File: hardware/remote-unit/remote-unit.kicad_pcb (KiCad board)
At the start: 2 copper layers, 100.6 x 51.3 mm, 49 parts, among them J1 SOL_A, J2 RF Module, J3 ICSP, J4 IO, J5 SOL_B, J6 PWR 12V, J7 UART, J8 I2C, SW1 RESET, U1 ATmega328P-AU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

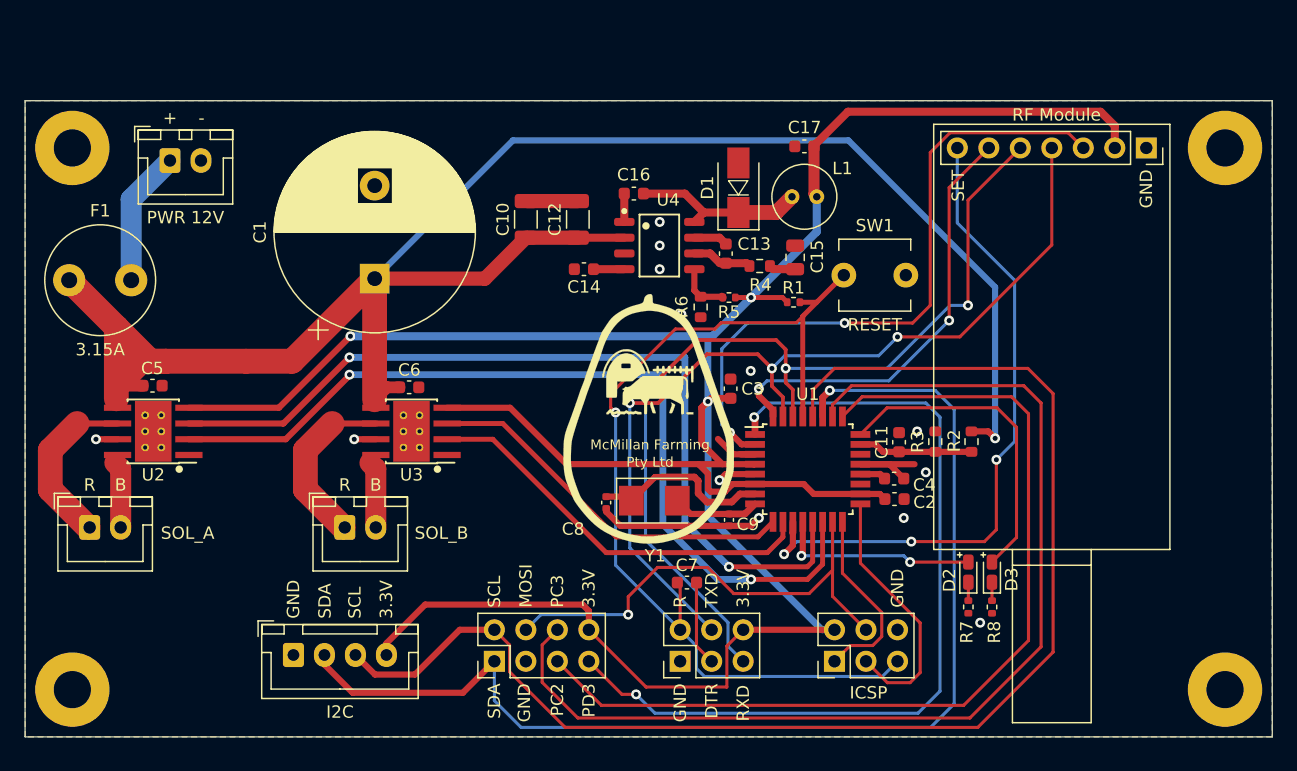
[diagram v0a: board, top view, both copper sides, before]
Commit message: Update inductor footprint on remote unit
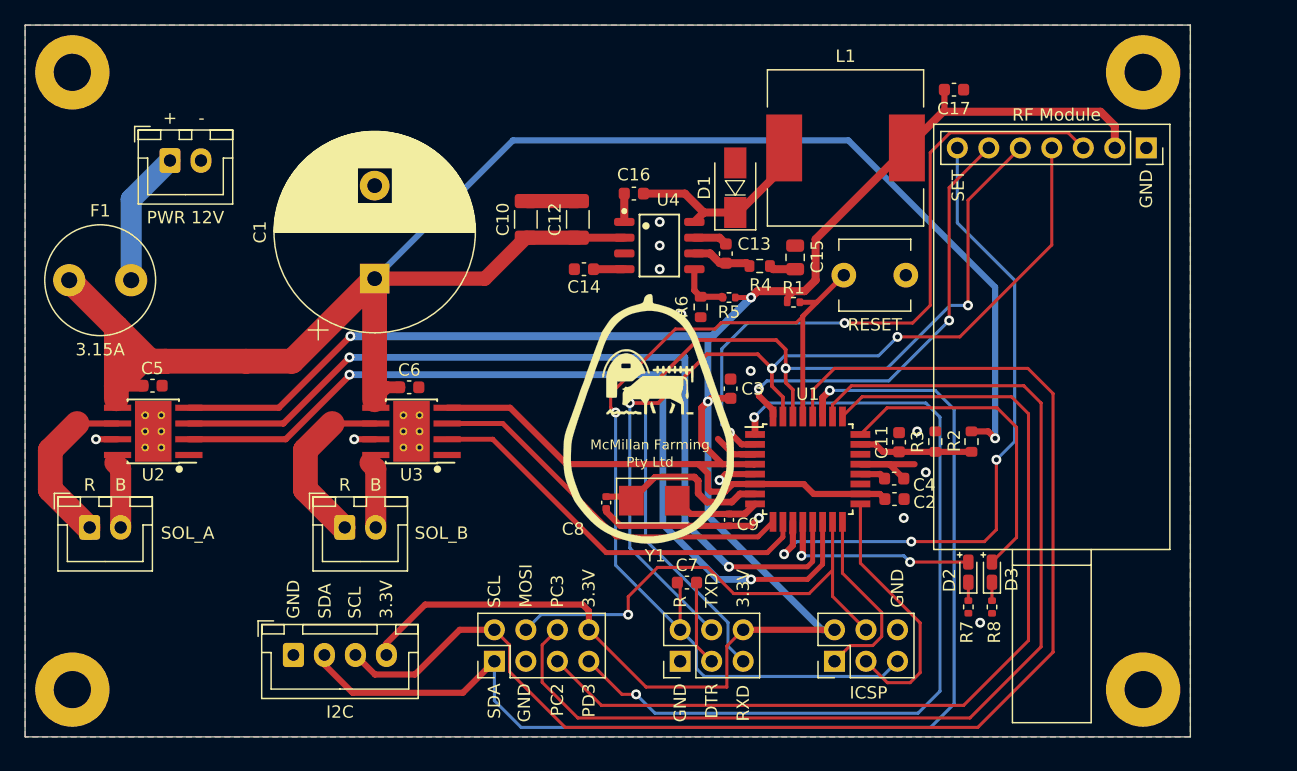
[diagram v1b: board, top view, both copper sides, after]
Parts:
- L1: footprint Capacitor_THT:C_Radial_D5.0mm_H7.0mm_P2.00mm -> Inductor_SMD:L_12x12mm_H8mm
- moved C17 12.9 mm to (157.2, 71.8), turned to 0 degrees
- moved H4 8.99 mm to (172.5, 70.4)
- moved H1 6.60 mm to (172.5, 120.1)
- moved H3 6.10 mm to (86.1, 70.4)
- moved L1 5.84 mm to (148.5, 76.5)
- moved D1 0.25 mm to (139.6, 79.7)
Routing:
- net Net-(C16-Pad1): track 14.2 -> 17.5 mm
- net +3V3: track 222.1 -> 220.5 mm
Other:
- board size 100.6 x 51.3 mm -> 94 x 57.4 mm

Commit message: Add boost converter for solar panel
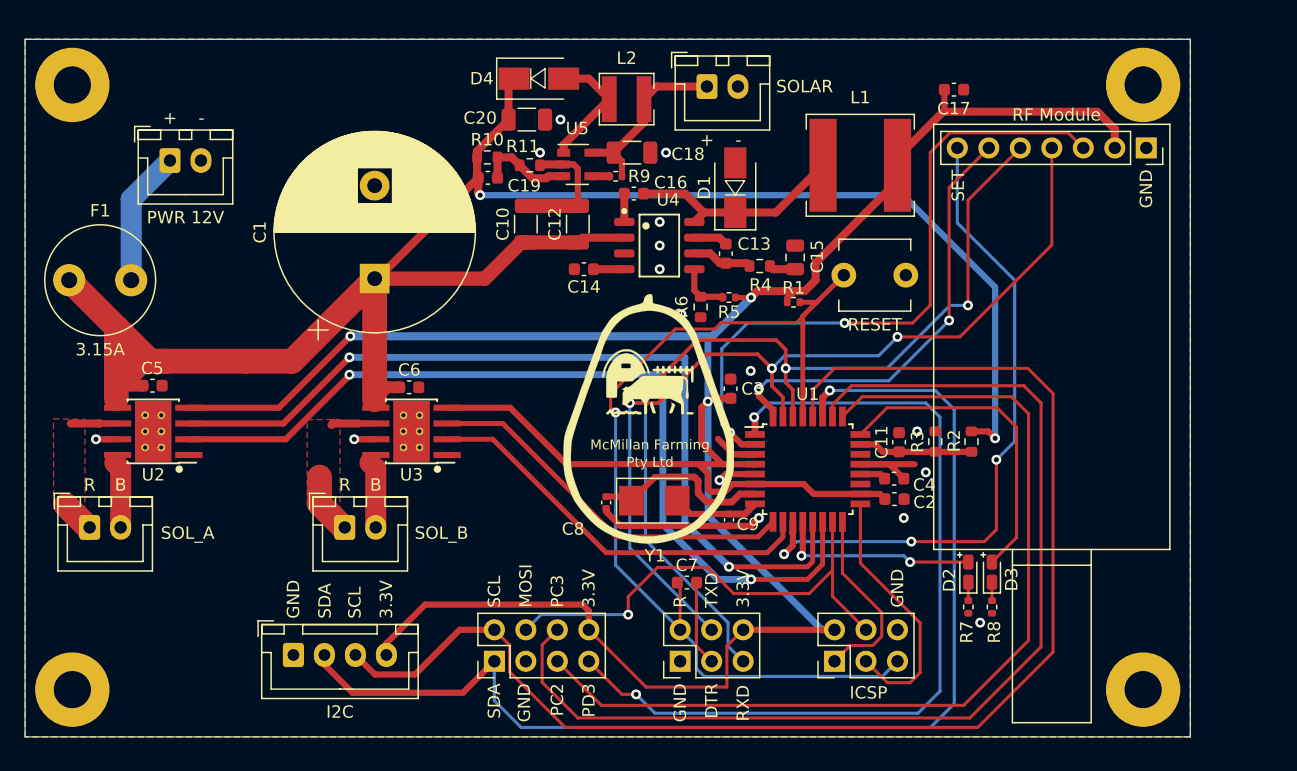
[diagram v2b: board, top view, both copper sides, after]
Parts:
- added C18: 10uF, Capacitor_SMD:C_1206_3216Metric, F.Cu at (131.2, 76.8)
- added C19: 200pF, Capacitor_SMD:C_0603_1608Metric, F.Cu at (119.6, 78.9)
- added C20: 10uF, Capacitor_SMD:C_1206_3216Metric, F.Cu at (122.8, 74.2)
- added D4: 550mV 1A, Diode_SMD:D_SMA, F.Cu at (123.7, 70.9)
- added J9: SOLAR, Connector_JST:JST_XH_B2B-XH-A_1x02_P2.50mm_Vertical, F.Cu at (137.3, 71.5)
- added L2: 10uH, lib:L_4x4mm_H2mm, F.Cu at (130.8, 72.5)
- added R10: 130k, Resistor_SMD:R_0603_1608Metric, F.Cu at (119.6, 77.2)
- added R11: 13k, Resistor_SMD:R_0603_1608Metric, F.Cu at (123.0, 77.9)
- added R9: 51k, Resistor_SMD:R_0402_1005Metric, F.Cu at (129.9, 78.7)
- added U5: LM27313XMF, Package_TO_SOT_SMD:SOT-23-5, F.Cu at (126.8, 77.8)
- L1: footprint Inductor_SMD:L_12x12mm_H8mm -> lib:L_8x8mm_H4mm
- moved L1 1.84 mm to (149.7, 77.9)
- moved H3 1.02 mm to (86.1, 71.4)
- moved H4 1.02 mm to (172.5, 71.4)
- moved C10 0.38 mm to (122.7, 82.6)
- moved C12 0.38 mm to (126.9, 82.6)
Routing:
- net /SOLAR: track 0.00 -> 14.8 mm
- net Net-(D4-Pad2): track 0.00 -> 10.2 mm
- net Net-(C19-Pad2): track 0.00 -> 7.75 mm
- net /SOL_A1: track 13.8 -> 6.29 mm
- net +12V: track 149.4 -> 156.9 mm, vias 1 -> 2
- net GND: track 39.7 -> 45.9 mm, vias 13 -> 16
- net /SOL_B1: track 14.2 -> 8.49 mm
- net Net-(R9-Pad2): track 0.00 -> 1.49 mm
- net Net-(C16-Pad1): track 17.5 -> 18.0 mm
- added copper zone on F.Cu, net /SOL_A1
- added copper zone on F.Cu, net /SOL_B1
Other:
- board size 94 x 57.4 mm -> 94 x 56.3 mm
- board text added: "Daniel McMillan 2021"

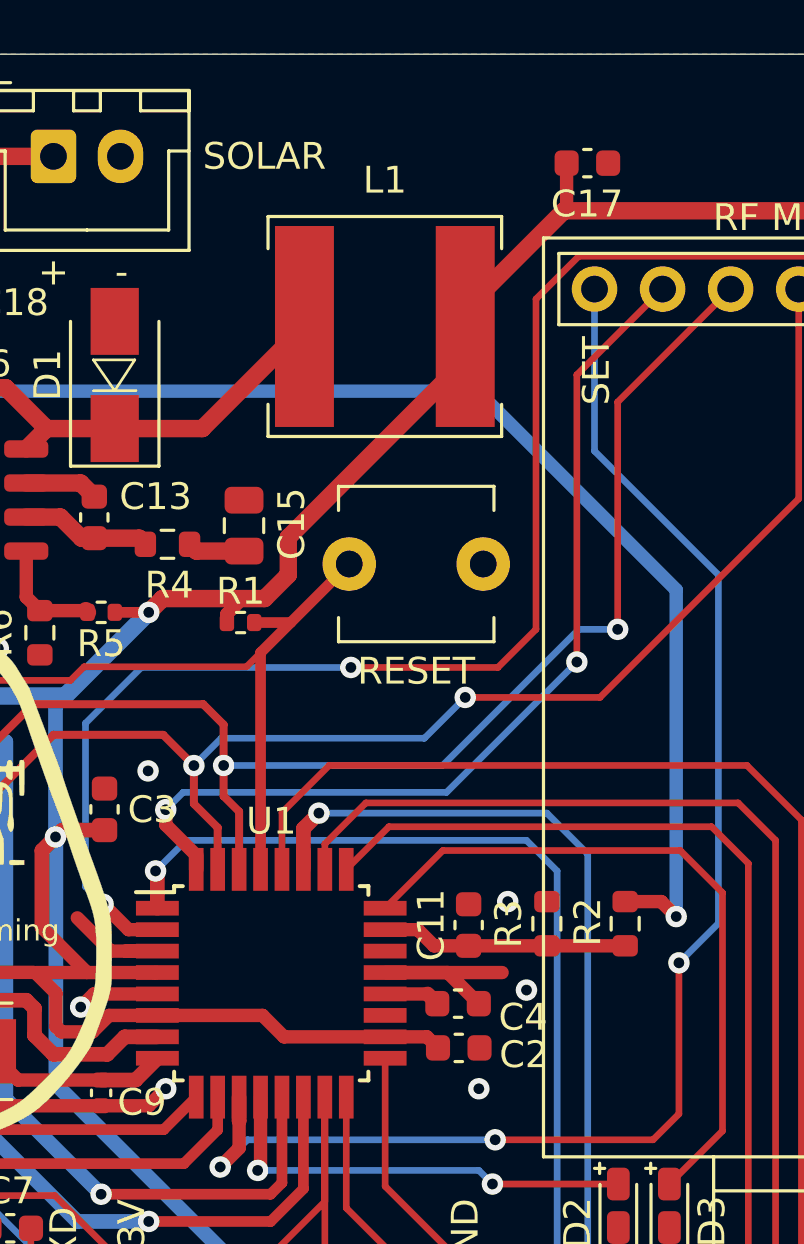
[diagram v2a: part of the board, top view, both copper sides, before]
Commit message: Fix remote unit buck converter
Compensation capacitor value was wrong.
Move output capacitor closer.
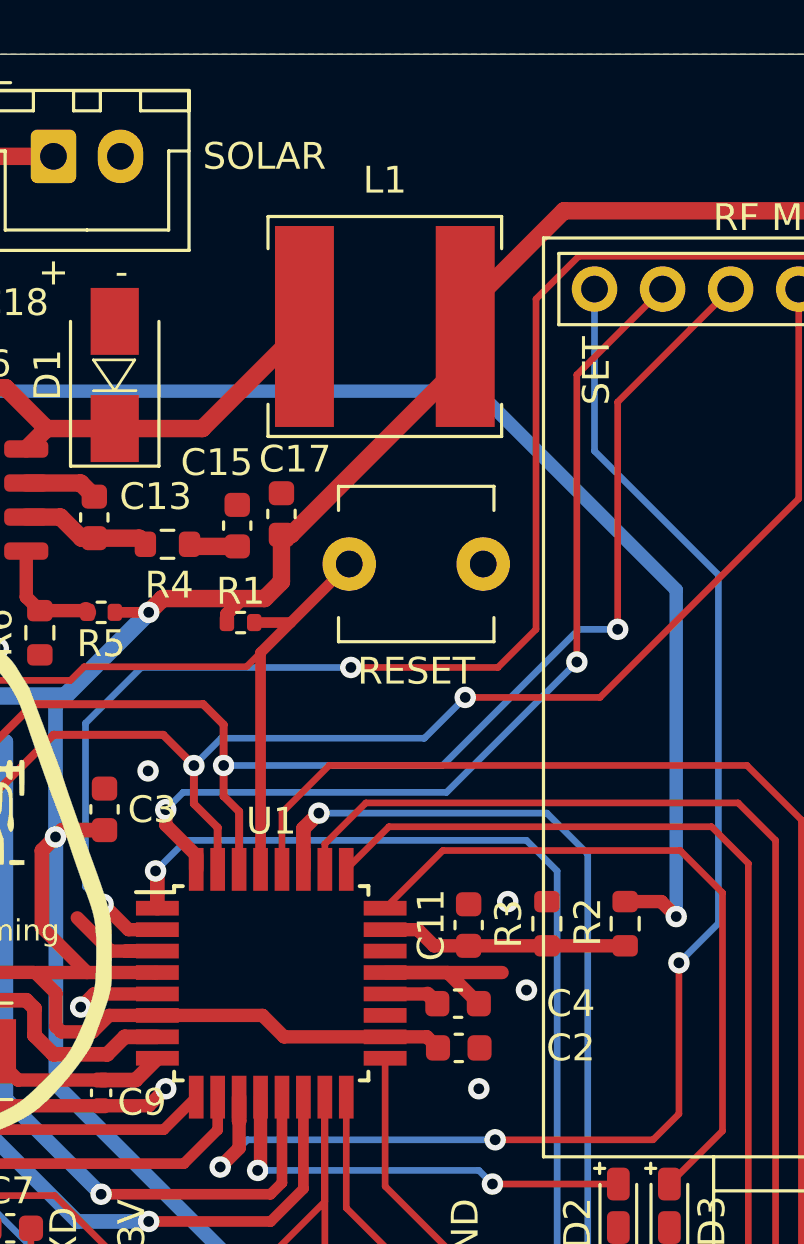
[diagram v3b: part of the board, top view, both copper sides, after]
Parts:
- C15: value 22uF 25V -> 22nF 25V; footprint Capacitor_SMD:C_0805_2012Metric -> Capacitor_SMD:C_0603_1608Metric
- moved C17 17.4 mm to (145.8, 84.8), turned to 90 degrees
- moved C15 0.25 mm to (144.1, 85.3)
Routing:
- net +3V3: track 220.2 -> 218.6 mm

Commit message: Update remote unit PCB
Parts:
- removed C18, C20: 10uF, Capacitor_SMD:C_1206_3216Metric
- removed C19: 200pF, Capacitor_SMD:C_0603_1608Metric
- removed J4: IO, Connector_PinHeader_2.54mm:PinHeader_2x04_P2.54mm_Vertical
- removed L2: 10uH, lib:L_4x4mm_H2mm
- added Q1: N >1A@4VGS, Package_TO_SOT_SMD:SOT-23-3, F.Cu at (126.2, 110.2)
- added Q2: PNP, Package_TO_SOT_SMD:SOT-23, F.Cu at (126.3, 114.2)
- added Q3: PNP, Package_TO_SOT_SMD:SOT-23, F.Cu at (99.3, 104.5)
- added Q4: NPN, Package_TO_SOT_SMD:SOT-23, F.Cu at (105.6, 112.0)
- added R12: 10k, Resistor_SMD:R_0402_1005Metric, F.Cu at (106.9, 115.1)
- added R13: 20k, Resistor_SMD:R_0402_1005Metric, F.Cu at (98.3, 107.7)
- D2, D3: footprint LED_SMD:LED_0603_1608Metric_Castellated -> LED_SMD:LED_0603_1608Metric
- J8: value I2C -> RS485
- R10: value 130k -> 220k
- R11: value 13k -> 10k; footprint Resistor_SMD:R_0603_1608Metric -> Resistor_SMD:R_0402_1005Metric
- R9: value 51k -> 220k; footprint Resistor_SMD:R_0402_1005Metric -> Resistor_SMD:R_0603_1608Metric
- U5: value LM27313XMF -> MAX3485; footprint Package_TO_SOT_SMD:SOT-23-5 -> Package_DIP:DIP-8_W7.62mm
- moved D4 44.5 mm to (130.6, 114.8), turned to -90 degrees
- moved J9 40.1 mm to (117.1, 106.2)
- moved R11 37.3 mm to (100.6, 107.7), turned to -90 degrees
- moved U5 36.2 mm to (119.4, 113.2), turned to -90 degrees
- moved R10 35.7 mm to (122.7, 112.8), turned to 180 degrees
- moved R9 28.9 mm to (123.4, 106.9), turned to 90 degrees
- moved J8 8.44 mm to (95.5, 117.0)
- moved J5 2.33 mm to (106.0, 106.0)
- moved J1 1.06 mm to (87.5, 106.0)
- moved C7 0.76 mm to (135.7, 112.3)
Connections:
- C17 pad 1: +3V3 -> +3.3V
- C2 pad 1: +3V3 -> +3.3V
- C3 pad 1: +3V3 -> +3.3V
- D4 pad 1: +12V -> Net-(D4-K)
- D4 pad 2: Net-(D4-Pad2) -> GND
- J2 pad 2: +3V3 -> +3.3V
- J3 pad 2: +3V3 -> +3.3V
- J7 pad 6: +3V3 -> +3.3V
- J8 pad 1: GND -> Net-(J8-Pin_1)
- J8 pad 2: /SDA -> Net-(J8-Pin_2)
- J8 pad 3: /SCL -> Net-(J8-Pin_3)
- J8 pad 4: +3V3 -> GND
- J9 pad 1: /SOLAR -> +12V
- J9 pad 2: GND -> /SOLAR_LOW
- L1 pad 2: +3V3 -> +3.3V
- R1 pad 1: +3V3 -> +3.3V
- R10 pad 1: +12V -> Net-(Q2-B)
- R10 pad 2: Net-(C19-Pad2) -> /PC4
- R11 pad 1: Net-(C19-Pad2) -> Net-(Q3-B)
- R11 pad 2: GND -> Net-(Q4-C)
- R5 pad 1: +3V3 -> +3.3V
- R9 pad 1: /SOLAR -> Net-(Q1-G)
- R9 pad 2: Net-(R9-Pad2) -> /SOLAR_LOW
- U1 pad 18: +3V3 -> +3.3V
- U1 pad 19: Net-(U1-Pad19) -> unconnected-(U1-ADC6-Pad19)
- U1 pad 22: Net-(U1-Pad22) -> unconnected-(U1-ADC7-Pad22)
- U1 pad 27: /SDA -> /PC4
- U1 pad 28: /SCL -> /PC5
- U1 pad 4: +3V3 -> +3.3V
- U1 pad 6: +3V3 -> +3.3V
- U2 pad 4: +3V3 -> +3.3V
- U3 pad 4: +3V3 -> +3.3V
- U4 pad 3: Net-(U4-Pad3) -> unconnected-(U4-EN-Pad3)
- U5 pad 1: Net-(D4-Pad2) -> /PC2
- U5 pad 2: GND -> /PC5
- U5 pad 3: Net-(C19-Pad2) -> /PC5
- U5 pad 4: Net-(R9-Pad2) -> /PD3
- U5 pad 5: /SOLAR -> GND
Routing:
- net +3V3: track 218.6 -> 0.00 mm, vias 3 -> 0
- net +3.3V: track 0.00 -> 202.7 mm, vias 0 -> 3
- net /SCL: track 109.4 -> 0.00 mm
- net /PC5: track 0.00 -> 101.9 mm, vias 0 -> 1
- net /SDA: track 95.2 -> 0.00 mm, vias 1 -> 0
- net /PC4: track 0.00 -> 81.8 mm, vias 0 -> 2
- net +12V: track 156.9 -> 199.9 mm, vias 2 -> 3
- net /MOSI: track 43.0 -> 9.82 mm, vias 1 -> 0
- net Net-(J8-Pin_2): track 0.00 -> 22.3 mm
- net Net-(J8-Pin_1): track 0.00 -> 18.2 mm, vias 0 -> 1
- net /PD3: track 70.2 -> 88.2 mm
- net Net-(J8-Pin_3): track 0.00 -> 16.0 mm
- net /SOLAR: track 14.8 -> 0.00 mm
- net /PC3: track 87.2 -> 101.0 mm
- net Net-(D4-Pad2): track 10.2 -> 0.00 mm
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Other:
- net class Default removed
- net class Power removed
- board text added: "Daniel McMillan 2023"
- board text removed: "Daniel McMillan 2021"
